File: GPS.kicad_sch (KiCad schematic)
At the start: 14 parts, among them Q3 Q_NMOS_DGS, Q4 Q_PMOS_DGS, U10 L96-M33

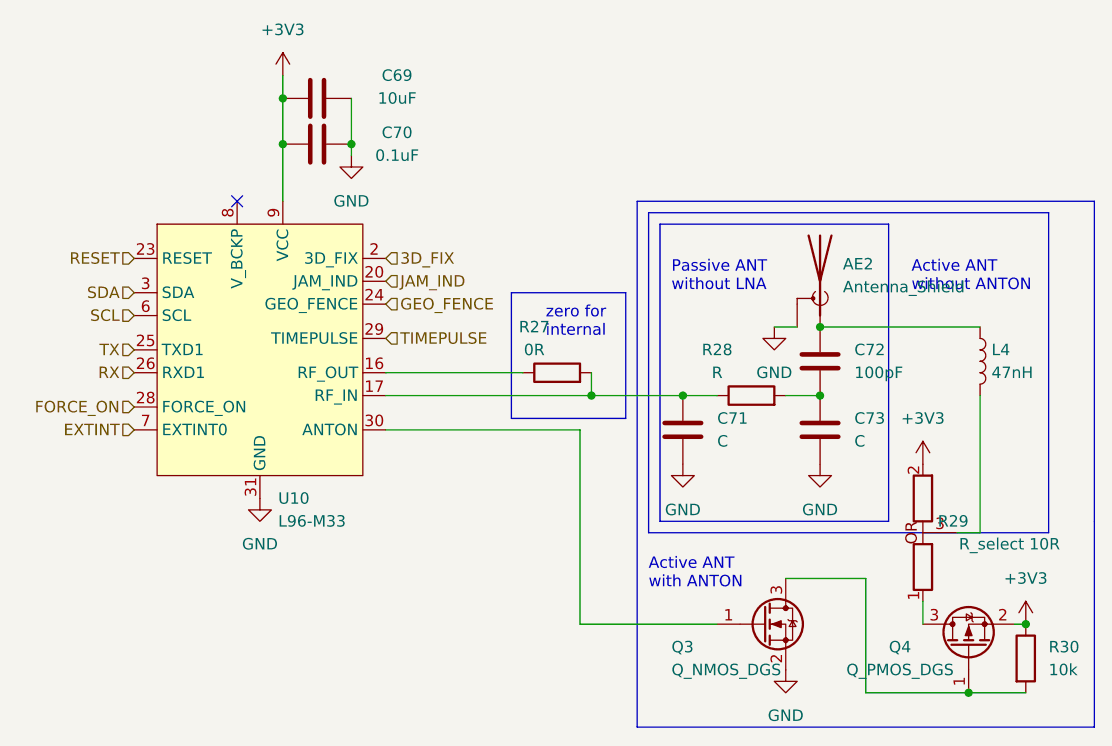
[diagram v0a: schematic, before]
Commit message: done first iteration of pcb routing, slikscreen still broken
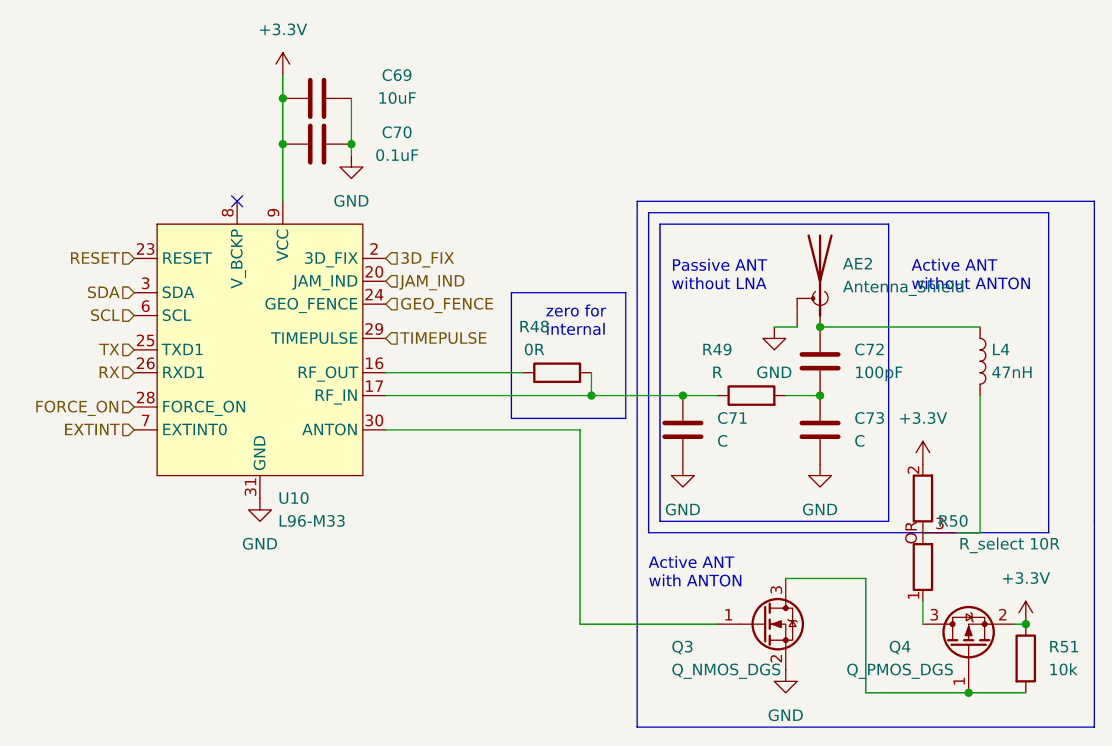
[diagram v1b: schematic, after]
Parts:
- renumbered R27 to R48, R28 to R49, R29 to R50, R30 to R51
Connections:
- net +3V3 renamed +3.3V
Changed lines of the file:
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@@
   (junction (at 149.86 64.77) (diameter 0) (color 0 0 0 0)
   )
+  (junction (at 176.53 92.71) (diameter 0) (color 0 0 0 0)
+  )
+  (junction (at 218.44 125.73) (diameter 0) (color 0 0 0 0)
+  )
+  (junction (at 201.93 92.71) (diameter 0) (color 0 0 0 0)
+  )
+  (junction (at 201.93 85.09) (diameter 0) (color 0 0 0 0)
+  )
   (junction (at 224.79 118.11) (diameter 0) (color 0 0 0 0)
-  )
-  (junction (at 176.53 92.71) (diameter 0) (color 0 0 0 0)
-  )
-  (junction (at 218.44 125.73) (diameter 0) (color 0 0 0 0)
-  )
-  (junction (at 201.93 92.71) (diameter 0) (color 0 0 0 0)
-  )
-  (junction (at 201.93 85.09) (diameter 0) (color 0 0 0 0)
   )
   (no_connect (at 137.16 71.12))
@@
     (effects (font (size 1.27 1.27)) (justify right))
   )
+  (symbol (lib_id "power:+3.3V") (at 213.36 100.33 0) (unit 1)
+    (in_bom yes) (on_board yes) (fields_autoplaced)
+    (property "Reference" "#PWR0229" (id 0) (at 213.36 104.14 0)
+      (effects (font (size 1.27 1.27)) hide)
+    )
+    (property "Value" "+3.3V" (id 1) (at 213.36 95.25 0))
+    (property "Footprint" "" (id 2) (at 213.36 100.33 0)
+      (effects (font (size 1.27 1.27)) hide)
+    )
+    (property "Datasheet" "" (id 3) (at 213.36 100.33 0)
+      (effects (font (size 1.27 1.27)) hide)
+    )
+    (pin "1")
+  )
   (symbol (lib_id "Device:R") (at 172.72 90.17 90) (unit 1)
     (in_bom yes) (on_board yes)
-    (property "Reference" "R27" (id 0) (at 170.18 85.09 90))
+    (property "Reference" "R48" (id 0) (at 170.18 85.09 90))
     (property "Value" "0R" (id 1) (at 170.18 87.63 90))
     (property "Footprint" "Resistor_SMD:R_0603_1608Metric_Pad0.98x0.95mm_HandSolder" (id 2) (at 172.72 91.948 90)
@@
   (symbol (lib_id "power:GND") (at 201.93 100.33 0) (unit 1)
     (in_bom yes) (on_board yes) (fields_autoplaced)
-    (property "Reference" "#PWR087" (id 0) (at 201.93 106.68 0)
+    (property "Reference" "#PWR090" (id 0) (at 201.93 106.68 0)
       (effects (font (size 1.27 1.27)) hide)
     )
@@
     (pin "1")
     (pin "2")
-  )
-  (symbol (lib_id "power:+3V3") (at 213.36 100.33 0) (unit 1)
-    (in_bom yes) (on_board yes) (fields_autoplaced)
-    (property "Reference" "#PWR088" (id 0) (at 213.36 104.14 0)
-      (effects (font (size 1.27 1.27)) hide)
-    )
-    (property "Value" "+3V3" (id 1) (at 213.36 95.25 0))
-    (property "Footprint" "" (id 2) (at 213.36 100.33 0)
-      (effects (font (size 1.27 1.27)) hide)
-    )
-    (property "Datasheet" "" (id 3) (at 213.36 100.33 0)
-      (effects (font (size 1.27 1.27)) hide)
-    )
-    (pin "1")
   )
   (symbol (lib_id "Device:C") (at 146.05 64.77 270) (mirror x) (unit 1)
@@
   (symbol (lib_id "power:GND") (at 196.85 85.09 0) (unit 1)
     (in_bom yes) (on_board yes) (fields_autoplaced)
-    (property "Reference" "#PWR085" (id 0) (at 196.85 91.44 0)
+    (property "Reference" "#PWR088" (id 0) (at 196.85 91.44 0)
       (effects (font (size 1.27 1.27)) hide)
     )
@@
   (symbol (lib_id "power:GND") (at 186.69 100.33 0) (unit 1)
     (in_bom yes) (on_board yes) (fields_autoplaced)
-    (property "Reference" "#PWR084" (id 0) (at 186.69 106.68 0)
+    (property "Reference" "#PWR087" (id 0) (at 186.69 106.68 0)
       (effects (font (size 1.27 1.27)) hide)
     )
@@
   (symbol (lib_id "airsoft_controller:R_select") (at 213.36 107.95 180) (unit 1)
     (in_bom yes) (on_board yes)
-    (property "Reference" "R29" (id 0) (at 218.44 106.68 0)
+    (property "Reference" "R50" (id 0) (at 218.44 106.68 0)
       (effects (font (size 1.27 1.27)) (justify left))
     )
@@
     (pin "2")
   )
+  (symbol (lib_id "power:+3.3V") (at 224.79 118.11 0) (unit 1)
+    (in_bom yes) (on_board yes) (fields_autoplaced)
+    (property "Reference" "#PWR0230" (id 0) (at 224.79 121.92 0)
+      (effects (font (size 1.27 1.27)) hide)
+    )
+    (property "Value" "+3.3V" (id 1) (at 224.79 113.03 0))
+    (property "Footprint" "" (id 2) (at 224.79 118.11 0)
+      (effects (font (size 1.27 1.27)) hide)
+    )
+    (property "Datasheet" "" (id 3) (at 224.79 118.11 0)
+      (effects (font (size 1.27 1.27)) hide)
+    )
+    (pin "1")
+  )
   (symbol (lib_id "Device:C") (at 186.69 96.52 0) (unit 1)
     (in_bom yes) (on_board yes) (fields_autoplaced)
@@
   (symbol (lib_id "power:GND") (at 139.7 104.14 0) (unit 1)
     (in_bom yes) (on_board yes) (fields_autoplaced)
-    (property "Reference" "#PWR081" (id 0) (at 139.7 110.49 0)
+    (property "Reference" "#PWR084" (id 0) (at 139.7 110.49 0)
       (effects (font (size 1.27 1.27)) hide)
     )
@@
     (pin "3")
   )
-  (symbol (lib_id "power:+3V3") (at 142.24 57.15 0) (mirror y) (unit 1)
-    (in_bom yes) (on_board yes) (fields_autoplaced)
-    (property "Reference" "#PWR082" (id 0) (at 142.24 60.96 0)
-      (effects (font (size 1.27 1.27)) hide)
-    )
-    (property "Value" "+3V3" (id 1) (at 142.24 52.07 0))
-    (property "Footprint" "" (id 2) (at 142.24 57.15 0)
-      (effects (font (size 1.27 1.27)) hide)
-    )
-    (property "Datasheet" "" (id 3) (at 142.24 57.15 0)
-      (effects (font (size 1.27 1.27)) hide)
-    )
-    (pin "1")
-  )
   (symbol (lib_id "Device:C") (at 146.05 59.69 270) (mirror x) (unit 1)
     (in_bom yes) (on_board yes)
@@
   (symbol (lib_id "power:GND") (at 149.86 66.04 0) (mirror y) (unit 1)
     (in_bom yes) (on_board yes) (fields_autoplaced)
-    (property "Reference" "#PWR083" (id 0) (at 149.86 72.39 0)
+    (property "Reference" "#PWR086" (id 0) (at 149.86 72.39 0)
       (effects (font (size 1.27 1.27)) hide)
     )
@@
     (pin "1")
   )
-  (symbol (lib_id "power:+3V3") (at 224.79 118.11 0) (unit 1)
-    (in_bom yes) (on_board yes) (fields_autoplaced)
-    (property "Reference" "#PWR089" (id 0) (at 224.79 121.92 0)
-      (effects (font (size 1.27 1.27)) hide)
-    )
-    (property "Value" "+3V3" (id 1) (at 224.79 113.03 0))
-    (property "Footprint" "" (id 2) (at 224.79 118.11 0)
-      (effects (font (size 1.27 1.27)) hide)
-    )
-    (property "Datasheet" "" (id 3) (at 224.79 118.11 0)
-      (effects (font (size 1.27 1.27)) hide)
-    )
-    (pin "1")
-  )
   (symbol (lib_id "Device:R") (at 224.79 121.92 0) (unit 1)
     (in_bom yes) (on_board yes) (fields_autoplaced)
-    (property "Reference" "R30" (id 0) (at 227.33 120.6499 0)
+    (property "Reference" "R51" (id 0) (at 227.33 120.6499 0)
       (effects (font (size 1.27 1.27)) (justify left))
     )
@@
     (pin "2")
   )
+  (symbol (lib_id "power:+3.3V") (at 142.24 57.15 0) (unit 1)
+    (in_bom yes) (on_board yes) (fields_autoplaced)
+    (property "Reference" "#PWR0228" (id 0) (at 142.24 60.96 0)
+      (effects (font (size 1.27 1.27)) hide)
+    )
+    (property "Value" "+3.3V" (id 1) (at 142.24 52.07 0))
+    (property "Footprint" "" (id 2) (at 142.24 57.15 0)
+      (effects (font (size 1.27 1.27)) hide)
+    )
+    (property "Datasheet" "" (id 3) (at 142.24 57.15 0)
+      (effects (font (size 1.27 1.27)) hide)
+    )
+    (pin "1")
+  )
   (symbol (lib_id "Device:R") (at 194.31 92.71 90) (unit 1)
     (in_bom yes) (on_board yes)
-    (property "Reference" "R28" (id 0) (at 190.5 87.63 90))
+    (property "Reference" "R49" (id 0) (at 190.5 87.63 90))
     (property "Value" "R" (id 1) (at 190.5 90.17 90))
     (property "Footprint" "Resistor_SMD:R_0603_1608Metric_Pad0.98x0.95mm_HandSolder" (id 2) (at 194.31 94.488 90)
@@
   (symbol (lib_id "power:GND") (at 198.12 123.19 0) (unit 1)
     (in_bom yes) (on_board yes) (fields_autoplaced)
-    (property "Reference" "#PWR086" (id 0) (at 198.12 129.54 0)
-      (effects (font (size 1.27 1.27)) hide)
-    )
+    (property "Reference" "#PWR089" (id 0) (at 198.12 129.54 0)
+      (effects (font (size 1.27 1.27)) hide)
+    )

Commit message: mounting holes, fixes silkscreen
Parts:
- renumbered R48 to R47, R49 to R48, R50 to R49, R51 to R50
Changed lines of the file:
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@@
   (symbol (lib_id "power:+3.3V") (at 213.36 100.33 0) (unit 1)
     (in_bom yes) (on_board yes) (fields_autoplaced)
-    (property "Reference" "#PWR0229" (id 0) (at 213.36 104.14 0)
+    (property "Reference" "#PWR091" (id 0) (at 213.36 104.14 0)
       (effects (font (size 1.27 1.27)) hide)
     )
@@
   (symbol (lib_id "Device:R") (at 172.72 90.17 90) (unit 1)
     (in_bom yes) (on_board yes)
-    (property "Reference" "R48" (id 0) (at 170.18 85.09 90))
+    (property "Reference" "R47" (id 0) (at 170.18 85.09 90))
     (property "Value" "0R" (id 1) (at 170.18 87.63 90))
     (property "Footprint" "Resistor_SMD:R_0603_1608Metric_Pad0.98x0.95mm_HandSolder" (id 2) (at 172.72 91.948 90)
@@
   (symbol (lib_id "airsoft_controller:R_select") (at 213.36 107.95 180) (unit 1)
     (in_bom yes) (on_board yes)
-    (property "Reference" "R50" (id 0) (at 218.44 106.68 0)
+    (property "Reference" "R49" (id 0) (at 218.44 106.68 0)
       (effects (font (size 1.27 1.27)) (justify left))
     )
@@
   (symbol (lib_id "power:+3.3V") (at 224.79 118.11 0) (unit 1)
     (in_bom yes) (on_board yes) (fields_autoplaced)
-    (property "Reference" "#PWR0230" (id 0) (at 224.79 121.92 0)
+    (property "Reference" "#PWR092" (id 0) (at 224.79 121.92 0)
       (effects (font (size 1.27 1.27)) hide)
     )
@@
   (symbol (lib_id "Device:R") (at 224.79 121.92 0) (unit 1)
     (in_bom yes) (on_board yes) (fields_autoplaced)
-    (property "Reference" "R51" (id 0) (at 227.33 120.6499 0)
+    (property "Reference" "R50" (id 0) (at 227.33 120.6499 0)
       (effects (font (size 1.27 1.27)) (justify left))
     )
@@
   (symbol (lib_id "power:+3.3V") (at 142.24 57.15 0) (unit 1)
     (in_bom yes) (on_board yes) (fields_autoplaced)
-    (property "Reference" "#PWR0228" (id 0) (at 142.24 60.96 0)
+    (property "Reference" "#PWR085" (id 0) (at 142.24 60.96 0)
       (effects (font (size 1.27 1.27)) hide)
     )
@@
   (symbol (lib_id "Device:R") (at 194.31 92.71 90) (unit 1)
     (in_bom yes) (on_board yes)
-    (property "Reference" "R49" (id 0) (at 190.5 87.63 90))
+    (property "Reference" "R48" (id 0) (at 190.5 87.63 90))
     (property "Value" "R" (id 1) (at 190.5 90.17 90))
     (property "Footprint" "Resistor_SMD:R_0603_1608Metric_Pad0.98x0.95mm_HandSolder" (id 2) (at 194.31 94.488 90)
